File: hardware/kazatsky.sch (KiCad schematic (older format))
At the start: 21 parts, among them J1 CTRL, J2 HALL, J3 VMOT, J4 MOTOR, J5 ISP, J6 USB_OTG, U1 L7805, U2 ATmega328PB-AU, U3 CH340G, Y1 12M

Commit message: Adding ADC pin for measuring input voltage.
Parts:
- added R3: 3.4k, coddingtonbear:0805_Milling, symbol Device:R_Small
- added R4: 10.2k, coddingtonbear:0805_Milling, symbol Device:R_Small
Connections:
- net +VDC: now also R4.2
- net GND: now also R3.1
- net VMOT: now reaches U2.28 (PC5)
- net VMOT: now also R3.2, R4.1
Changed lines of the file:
@@
 Text GLabel 5450 5550 2    50   Input ~ 0
 CTRL_UP
+$Comp
+L power:+VDC #PWR0124
+U 1 1 5D9D5F4B
+P 3600 3100
+F 0 "#PWR0124" H 3600 3000 50  0001 C CNN
+F 1 "+VDC" H 3600 3375 50  0000 C CNN
+F 2 "" H 3600 3100 50  0001 C CNN
+F 3 "" H 3600 3100 50  0001 C CNN
+	1    3600 3100
+	1    0    0    -1
+$EndComp
+Text GLabel 5450 4950 2    50   Input ~ 0
+VMOT
+Text GLabel 3200 3400 3    50   Input ~ 0
+VMOT
+$Comp
+L Device:R_Small R4
+U 1 1 5D9D6127
+P 3350 3200
+F 0 "R4" V 3154 3200 50  0000 C CNN
+F 1 "10.2k" V 3245 3200 50  0000 C CNN
+F 2 "coddingtonbear:0805_Milling" H 3350 3200 50  0001 C CNN
+F 3 "~" H 3350 3200 50  0001 C CNN
+	1    3350 3200
+	0    -1   -1   0
+$EndComp
+$Comp
+L Device:R_Small R3
+U 1 1 5D9D61B7
+P 3050 3200
+F 0 "R3" V 2854 3200 50  0000 C CNN
+F 1 "3.4k" V 2945 3200 50  0000 C CNN
+F 2 "coddingtonbear:0805_Milling" H 3050 3200 50  0001 C CNN
+F 3 "~" H 3050 3200 50  0001 C CNN
+	1    3050 3200
+	0    -1   -1   0
+$EndComp
+$Comp
+L power:GND #PWR0125
+U 1 1 5D9D7D88
+P 2800 3200
+F 0 "#PWR0125" H 2800 2950 50  0001 C CNN
+F 1 "GND" H 2805 3027 50  0000 C CNN
+F 2 "" H 2800 3200 50  0001 C CNN
+F 3 "" H 2800 3200 50  0001 C CNN
+	1    2800 3200
+	1    0    0    -1
+$EndComp
+Wire Wire Line
+	3600 3100 3600 3200
+Wire Wire Line
+	3600 3200 3450 3200
+Wire Wire Line
+	2800 3200 2950 3200
+Wire Wire Line
+	3150 3200 3200 3200
+Wire Wire Line
+	3200 3200 3200 3400
+Connection ~ 3200 3200
+Wire Wire Line
+	3200 3200 3250 3200
 $EndSCHEMATC

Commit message: Updating to v2.0 of the board.
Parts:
- removed C5, C6: 22p, coddingtonbear:0805_Milling, symbol Device:C_Small
- removed J2: HALL, TerminalBlock:TerminalBlock_bornier-4_P5.08mm, symbol Connector_Generic:Conn_01x04
- removed J5: ISP, Connector_IDC:IDC-Header_2x03_P2.54mm_Vertical, symbol Connector_Generic:Conn_02x03_Odd_Even
- removed R1: 10k, coddingtonbear:0805_Milling, symbol Device:R_Small
- removed U3: CH340G, Package_SO:SOP-16_4.4x10.4mm_P1.27mm, symbol coddingtonbear:CH340G
- removed Y1: 12M, coddingtonbear:Crystal_HC49-U_Vertical_LargePads, symbol Device:Crystal
- added J2: HALL/LIMIT/RST, TerminalBlock_RND:TerminalBlock_RND_205-00238_1x08_P5.08mm_Horizontal, symbol Connector_Generic:Conn_01x08
- added U3: CH340B, Package_SO:SOIC-16_4.55x10.3mm_P1.27mm, symbol coddingtonbear:CH340B
- J6: symbol Connector:USB_OTG -> kazatsky-rescue:USB_OTG-Connector
- U2: symbol MCU_Microchip_ATmega:ATmega328PB-AU -> kazatsky-rescue:ATmega328PB-AU-MCU_Microchip_ATmega
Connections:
- net +5V: now also J2.8 (Pin_8), U3.16 (VCC)
- net GND: now also J2.5 (Pin_5), J2.7 (Pin_7), U3.1 (GND)
- net HALL: now also U2.23 (PC0), J2.6 (Pin_6); no longer U2.24 (PC1)
- net L_EN: now also U2.6 (PE1); no longer U2.11 (PD7)
- net RXD: now also U3.2 (TXD)
- net TXD: now also U3.3 (RXD)
- net UD+: now also U3.5 (UD+)
- net UD-: now also U3.6 (UD-)
- net USB_RESET: now also J2.2 (Pin_2); no longer C9.1
- net VMOT: now also U2.32 (PD2); no longer U2.28 (PC5)
- net at U2.25 (PC2): now also J2.3 (Pin_3)
- net at C9.2: now also U3.13 (DTR/)
- net at C7.1: now also U3.4 (V3)
- new net USB_RESET_DTR: C9.1, J2.1 (Pin_1)
- new net ~LIMIT: J2.4 (Pin_4), U2.24 (PC1)
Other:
- moved on the sheet: C2, C3, C4, J1, J3, J4, R2, R3, R4, U2

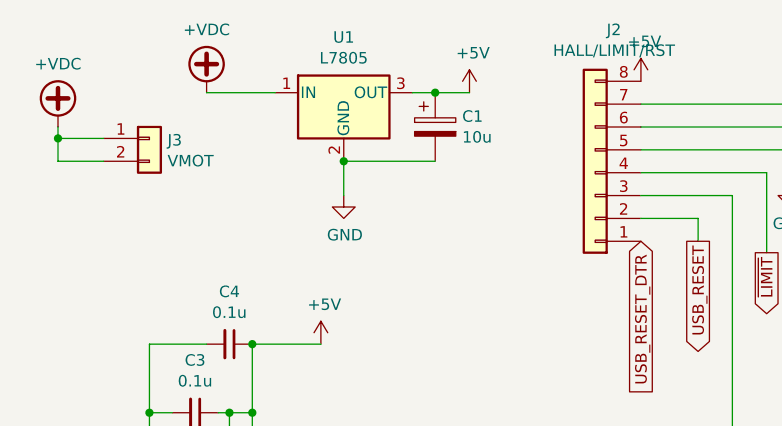
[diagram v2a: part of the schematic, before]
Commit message: Adding extra capacitance.
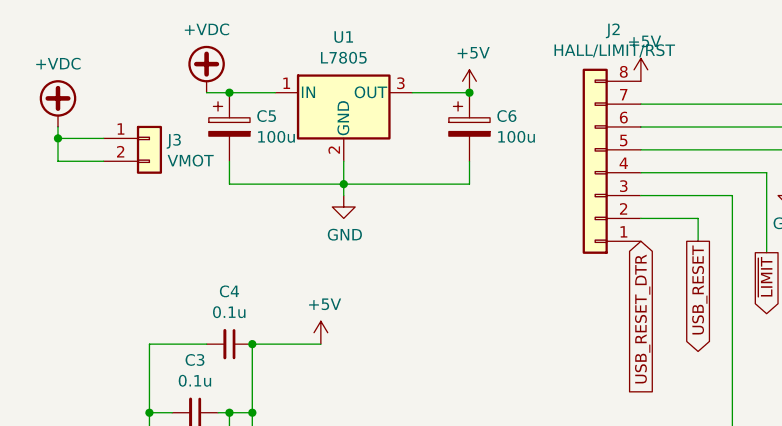
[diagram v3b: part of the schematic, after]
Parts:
- removed C1: 10u, coddingtonbear:CP_Tantalum_Case-D_EIA-7343-31_Milling, symbol Device:CP
- added C5, C6: 100u, Capacitor_SMD:CP_Elec_6.3x5.4, symbol Device:CP
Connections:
- net +5V: now also C6.1
- net +VDC: now also C5.1
- net GND: now also C5.2, C6.2
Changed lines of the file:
@@
 	1    0    0    -1
 $EndComp
-$Comp
-L Device:CP C1
-U 1 1 5D9CBBEC
-P 2550 1500
-F 0 "C1" H 2668 1546 50  0000 L CNN
-F 1 "10u" H 2668 1455 50  0000 L CNN
-F 2 "coddingtonbear:CP_Tantalum_Case-D_EIA-7343-31_Milling" H 2588 1350 50  0001 C CNN
-F 3 "~" H 2550 1500 50  0001 C CNN
-	1    2550 1500
-	1    0    0    -1
-$EndComp
-Wire Wire Line
-	2450 1350 2550 1350
-Wire Wire Line
-	2550 1350 2700 1350
-Connection ~ 2550 1350
-Wire Wire Line
-	2550 1650 2150 1650
-Wire Wire Line
-	2150 1650 2150 1800
-Connection ~ 2150 1650
-Wire Wire Line
-	1850 1350 1550 1350
+Wire Wire Line
+	2150 1650 2150 1750
+Wire Wire Line
+	1850 1350 1650 1350
 Text GLabel 2250 5550 2    50   Output ~ 0
 L_PWM
@@
 Wire Wire Line
 	3850 1800 3850 4450
+$Comp
+L Device:CP C5
+U 1 1 604D709B
+P 1650 1500
+F 0 "C5" H 1768 1546 50  0000 L CNN
+F 1 "100u" H 1768 1455 50  0000 L CNN
+F 2 "Capacitor_SMD:CP_Elec_6.3x5.4" H 1688 1350 50  0001 C CNN
+F 3 "~" H 1650 1500 50  0001 C CNN
+	1    1650 1500
+	1    0    0    -1
+$EndComp
+$Comp
+L Device:CP C6
+U 1 1 604D776E
+P 2700 1500
+F 0 "C6" H 2818 1546 50  0000 L CNN
+F 1 "100u" H 2818 1455 50  0000 L CNN
+F 2 "Capacitor_SMD:CP_Elec_6.3x5.4" H 2738 1350 50  0001 C CNN
+F 3 "~" H 2700 1500 50  0001 C CNN
+	1    2700 1500
+	1    0    0    -1
+$EndComp
+Wire Wire Line
+	2450 1350 2700 1350
+Connection ~ 2700 1350
+Connection ~ 1650 1350
+Wire Wire Line
+	1650 1350 1550 1350
+Wire Wire Line
+	1650 1650 1650 1750
+Wire Wire Line
+	1650 1750 2150 1750
+Connection ~ 2150 1750
+Wire Wire Line
+	2150 1750 2150 1800
+Wire Wire Line
+	2700 1650 2700 1750
+Wire Wire Line
+	2700 1750 2150 1750
 $EndSCHEMATC
